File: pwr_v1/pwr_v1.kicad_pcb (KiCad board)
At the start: 4 copper layers, 166 x 166 mm, 118 parts, among them CN11 Conn_02x36_Odd_Even, CN12 Conn_02x36_Odd_Even, M1 Conn_01x08_Socket, M2 Conn_01x08_Socket, M3 Conn_01x08_Socket, M4 Conn_01x08_Socket, M5 Conn_01x08_Socket, U1 LM2576S-5, U2 LM2576S-12, U4 LSM6DSLTR

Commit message: Schematic and layout updated; Layout placement and routing completed
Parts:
- removed the REF** at (118.0, 65.1)
- added 0R1: 0, Resistor_SMD:R_0603_1608Metric, F.Cu at (187.4, 125.0)
- added 0R10: 0, Resistor_SMD:R_0603_1608Metric, F.Cu at (126.8, 104.0)
- added 0R11: 0, Resistor_SMD:R_0603_1608Metric, F.Cu at (187.6, 119.4)
- added 0R12: 0, Resistor_SMD:R_0603_1608Metric, F.Cu at (173.2, 119.2)
- added 0R13: 0, Resistor_SMD:R_0603_1608Metric, F.Cu at (171.8, 128.6)
- added 0R14: 0, Resistor_SMD:R_0603_1608Metric, F.Cu at (127.2, 98.1)
- added 0R15: 0, Resistor_SMD:R_0603_1608Metric, F.Cu at (171.8, 131.1)
- added 0R16: 0, Resistor_SMD:R_0603_1608Metric, F.Cu at (126.2, 120.1)
- added 0R17: 0, Resistor_SMD:R_0603_1608Metric, F.Cu at (127.1, 125.9)
- added 0R18: 0, Resistor_SMD:R_0603_1608Metric, F.Cu at (111.4, 85.4)
- added 0R19: 0, Resistor_SMD:R_0603_1608Metric, F.Cu at (127.0, 123.5)
- added 0R2: 0, Resistor_SMD:R_0603_1608Metric, F.Cu at (127.0, 67.7)
- added 0R20: 0, Resistor_SMD:R_0603_1608Metric, F.Cu at (127.2, 141.3)
- added 0R21: 0, Resistor_SMD:R_0603_1608Metric, F.Cu at (173.2, 81.2)
- added 0R22: 0, Resistor_SMD:R_0603_1608Metric, F.Cu at (172.4, 77.8)
- added 0R23: 0, Resistor_SMD:R_0603_1608Metric, F.Cu at (171.8, 100.6)
- added 0R24: 0, Resistor_SMD:R_0603_1608Metric, F.Cu at (187.4, 94.6)
- added 0R25: 0, Resistor_SMD:R_0603_1608Metric, F.Cu at (187.6, 68.4)
- added 0R26: 0, Resistor_SMD:R_0603_1608Metric, F.Cu at (172.6, 67.6)
- added 0R27: 0, Resistor_SMD:R_0603_1608Metric, F.Cu at (188.0, 80.4)
- added 0R28: 0, Resistor_SMD:R_0603_1608Metric, F.Cu at (188.4, 77.8)
- added 0R29: 0, Resistor_SMD:R_0603_1608Metric, F.Cu at (127.2, 100.7)
- added 0R3: 0, Resistor_SMD:R_0603_1608Metric, F.Cu at (173.0, 86.4)
- added 0R30: 0, Resistor_SMD:R_0603_1608Metric, F.Cu at (172.2, 111.0)
- added 0R31: 0, Resistor_SMD:R_0603_1608Metric, F.Cu at (172.2, 108.4)
- added 0R32: 0, Resistor_SMD:R_0603_1608Metric, F.Cu at (187.4, 101.4)
- added 0R33: 0, Resistor_SMD:R_0603_1608Metric, F.Cu at (188.2, 85.4)
- added 0R34: 0, Resistor_SMD:R_0603_1608Metric, F.Cu at (172.2, 95.6)
- added 0R35: 0, Resistor_SMD:R_0603_1608Metric, F.Cu at (188.2, 83.0)
- added 0R36: 0, Resistor_SMD:R_0603_1608Metric, F.Cu at (171.8, 126.0)
- added 0R4: 0, Resistor_SMD:R_0603_1608Metric, F.Cu at (187.4, 90.6)
- added 0R5: 0, Resistor_SMD:R_0603_1608Metric, F.Cu at (187.4, 132.8)
- added 0R6: 0, Resistor_SMD:R_0603_1608Metric, F.Cu at (187.8, 143.0)
- added 0R7: 0, Resistor_SMD:R_0603_1608Metric, F.Cu at (187.2, 112.4)
- added 0R8: 0, Resistor_SMD:R_0603_1608Metric, F.Cu at (172.2, 116.0)
- added 0R9: 0, Resistor_SMD:R_0603_1608Metric, F.Cu at (171.8, 133.8)
- added ?: , , B.Cu at (215.0, 136.2)
- added ?: , , B.Cu at (180.2, 37.8)
- added ?: , , B.Cu at (83.0, 84.0)
- added ?: , , B.Cu at (134.8, 164.4)
- added Bat2: Conn_01x07, B7B_XH_A:JST_B7B-XH-A, F.Cu at (151.6, 153.6)
- added C5: 100uF, Capacitor_SMD:CP_Elec_8x10, B.Cu at (140.1, 128.6)
- added C6: 1000uF, Capacitor_SMD:CP_Elec_10x10.5, B.Cu at (160.4, 118.1)
- added D3: 1N5821, Diode_THT:D_DO-201AD_P15.24mm_Horizontal, B.Cu at (148.4, 119.3)
- added J1: Conn_01x12_Pin, 12pConn:CON12_1X12_UR_DF13, B.Cu at (222.1, 127.8)
- added L4: 100uH, Inductor_SMD:L_Sunlord_MWSA1206S-101, B.Cu at (147.4, 107.5)
- added Q1: BSS84, Package_TO_SOT_SMD:SOT-23, B.Cu at (215.0, 126.5)
- added R15: 1M, Resistor_SMD:R_0603_1608Metric, F.Cu at (171.0, 146.4)
- added R16: 100k, Resistor_SMD:R_0603_1608Metric, F.Cu at (171.0, 148.0)
- added REF**: TerminalBlock_MetzConnect_360271_1x01_Horizontal_ScrewM3.0_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, TerminalBlock_MetzConnect:TerminalBlock_MetzConnect_360271_1x01_Horizontal_ScrewM3.0_Boxed, F.Cu at (120.0, 36.0)
- added REF**: Fiducial_1mm_Mask2mm, Fiducial:Fiducial_1mm_Mask2mm, F.Cu at (83.0, 84.0)
- added REF**: Fiducial_1mm_Mask2mm, Fiducial:Fiducial_1mm_Mask2mm, F.Cu at (180.2, 37.8)
- added REF**: Fiducial_1mm_Mask2mm, Fiducial:Fiducial_1mm_Mask2mm, F.Cu at (215.0, 136.2)
- added REF**: TerminalBlock_MetzConnect_360271_1x01_Horizontal_ScrewM3.0_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, TerminalBlock_MetzConnect:TerminalBlock_MetzConnect_360271_1x01_Horizontal_ScrewM3.0_Boxed, F.Cu at (180.4, 164.0)
- added REF**: TerminalBlock_MetzConnect_360271_1x01_Horizontal_ScrewM3.0_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, TerminalBlock_MetzConnect:TerminalBlock_MetzConnect_360271_1x01_Horizontal_ScrewM3.0_Boxed, F.Cu at (119.4, 163.8)
- added REF**: TerminalBlock_MetzConnect_360271_1x01_Horizontal_ScrewM3.0_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, TerminalBlock_MetzConnect:TerminalBlock_MetzConnect_360271_1x01_Horizontal_ScrewM3.0_Boxed, F.Cu at (188.4, 36.0)
- added REF**: Fiducial_1mm_Mask2mm, Fiducial:Fiducial_1mm_Mask2mm, F.Cu at (134.8, 164.4)
- added RK1: 100, Resistor_SMD:R_0402_1005Metric, B.Cu at (219.7, 127.8)
- added RK10: 10k, Resistor_SMD:R_0402_1005Metric, B.Cu at (216.5, 120.2)
- added RK2: 100, Resistor_SMD:R_0402_1005Metric, B.Cu at (219.6, 126.5)
- added RK3: 100, Resistor_SMD:R_0402_1005Metric, B.Cu at (219.6, 125.3)
- added RK4: 100, Resistor_SMD:R_0402_1005Metric, B.Cu at (219.7, 124.1)
- added RK5: 100, Resistor_SMD:R_0402_1005Metric, B.Cu at (219.6, 122.7)
- added RK6: 100, Resistor_SMD:R_0402_1005Metric, B.Cu at (219.8, 121.5)
- added RK7: 100, Resistor_SMD:R_0402_1005Metric, B.Cu at (219.8, 120.3)
- added RK8: 100, Resistor_SMD:R_0402_1005Metric, B.Cu at (219.8, 118.9)
- added RK9: 10k, Resistor_SMD:R_0402_1005Metric, B.Cu at (216.5, 121.5)
- added U3: LM2576S-3.3, Package_TO_SOT_SMD:TO-263-5_TabPin3, B.Cu at (152.0, 133.3)
- J_IR1: footprint Connector_PinHeader_2.54mm:PinHeader_1x05_P2.54mm_Vertical -> Connector_PinHeader_2.54mm:PinHeader_1x05_P2.54mm_Vertical_SMD_Pin1Left; moved to B.Cu
- J_RF1: footprint Connector_PinHeader_2.54mm:PinHeader_2x04_P2.54mm_Vertical -> Connector_PinSocket_2.54mm:PinSocket_2x04_P2.54mm_Vertical
- M1, M2, M3, M4, M5: footprint Connector_Molex:Molex_KK-254_AE-6410-08A_1x08_P2.54mm_Vertical -> Connector_PinHeader_2.54mm:PinHeader_1x08_P2.54mm_Vertical; moved to B.Cu
- moved C1 139.7 mm to (217.5, 87.9), turned to 0 degrees
- moved U1 138.9 mm to (76.5, 98.0), turned to 180 degrees
- moved U2 132.6 mm to (222.3, 99.9), turned to 0 degrees
- moved C3 130.8 mm to (93.6, 90.0), turned to 90 degrees
- moved R14 127.9 mm to (156.6, 148.0), turned to 90 degrees
- moved R13 127.4 mm to (156.7, 144.8), turned to -90 degrees
- moved R12 127.2 mm to (154.1, 148.0), turned to 90 degrees
- moved R10 126.8 mm to (151.6, 147.9), turned to 90 degrees
- moved R4 126.8 mm to (144.1, 147.9), turned to 90 degrees
- moved R11 126.7 mm to (154.2, 144.8), turned to -90 degrees
- moved R8 126.7 mm to (149.2, 148.0), turned to 90 degrees
- moved R6 126.5 mm to (146.6, 148.0), turned to 90 degrees
- moved R9 126.2 mm to (151.6, 144.8), turned to -90 degrees
- moved R7 125.9 mm to (149.2, 144.8), turned to -90 degrees
- moved R1 125.9 mm to (144.1, 144.8), turned to -90 degrees
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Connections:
- C12 pad 1: /3V3 -> 3V3
- C13 pad 1: /3V3 -> 3V3
- CN11 pad 11: unconnected-(CN11-Pin_11-Pad11) -> /Battery Supervisor/O1
- CN11 pad 17: unconnected-(CN11-Pin_17-Pad17) -> /STM32/MOTOR5_ENCODER
- CN11 pad 19: unconnected-(CN11-Pin_19-Pad19) -> GND
- CN11 pad 22: unconnected-(CN11-Pin_22-Pad22) -> GND
- CN11 pad 23: /STM32/BTN_USER -> unconnected-(CN11-Pin_23-Pad23)
- CN11 pad 28: unconnected-(CN11-Pin_28-Pad28) -> /STM32/MOTOR4_ENCODER
- CN11 pad 30: unconnected-(CN11-Pin_30-Pad30) -> /STM32/IR_CS
- CN11 pad 32: unconnected-(CN11-Pin_32-Pad32) -> /STM32/MOTOR3_ENCODER
- CN11 pad 34: /STM32/LED_GREEN -> unconnected-(CN11-Pin_34-Pad34)
- CN11 pad 38: unconnected-(CN11-Pin_38-Pad38) -> /Battery Supervisor/O6
- CN11 pad 4: unconnected-(CN11-Pin_4-Pad4) -> /STM32/MOTOR1_ENCODER
- CN11 pad 46: /MotorDriver4/BRAKE -> /STM32/MOTOR4_BREAK
- CN11 pad 48: unconnected-(CN11-Pin_48-Pad48) -> /STM32/MOTOR5_REVERSE
- CN11 pad 49: unconnected-(CN11-Pin_49-Pad49) -> GND
- CN11 pad 50: unconnected-(CN11-Pin_50-Pad50) -> /STM32/MOTOR5_PWM
- CN11 pad 54: unconnected-(CN11-Pin_54-Pad54) -> /Battery Supervisor/O3
- CN11 pad 56: unconnected-(CN11-Pin_56-Pad56) -> /Battery Supervisor/O2
- CN11 pad 60: unconnected-(CN11-Pin_60-Pad60) -> GND
- CN11 pad 61: /STM32/LED_YELLOW -> unconnected-(CN11-Pin_61-Pad61)
- CN11 pad 62: unconnected-(CN11-Pin_62-Pad62) -> /STM32/MOTOR5_BREAK
- CN11 pad 8: unconnected-(CN11-Pin_8-Pad8) -> GND
- CN11 pad 9: /MotorDriver1/FGOUT -> /Battery Supervisor/O4
- CN12 pad 11: /SCK -> /STM32/SCK
- CN12 pad 12: unconnected-(CN12-Pin_12-Pad12) -> /STM32/IR_IN
- CN12 pad 13: /MISO -> /STM32/MISO
- CN12 pad 14: unconnected-(CN12-Pin_14-Pad14) -> /STM32/IR_OUT
- CN12 pad 15: /MOSI -> unconnected-(CN12-Pin_15-Pad15)
- CN12 pad 16: unconnected-(CN12-Pin_16-Pad16) -> /STM32/KICKER_DISCHARGE2
- CN12 pad 17: /MotorDriver1/DIR -> /STM32/MOTOR1_REVERSE
- CN12 pad 18: unconnected-(CN12-Pin_18-Pad18) -> /STM32/KICKER_CHARGE
- CN12 pad 20: unconnected-(CN12-Pin_20-Pad20) -> GND
- CN12 pad 22: /MotorDriver1/BRAKE -> /STM32/MOTOR1_BREAK
- CN12 pad 23: /MotorDriver1/PWM -> unconnected-(CN12-Pin_23-Pad23)
- CN12 pad 25: /STM32/KICKER_DISCHARGE -> /STM32/KICKER_DISCHARGE1
- CN12 pad 26: /RF/IRQ -> /STM32/NRF_IRQ
- CN12 pad 28: /STM32/LED_RED -> unconnected-(CN12-Pin_28-Pad28)
- CN12 pad 29: unconnected-(CN12-Pin_29-Pad29) -> /STM32/MOSI
- CN12 pad 3: /RF/CSN -> /STM32/CS_NRF
- CN12 pad 30: /MotorDriver2/DIR -> /STM32/KICKER_ERR
- CN12 pad 35: /MotorDriver3/FGOUT -> /STM32/IR_INT1
- CN12 pad 37: unconnected-(CN12-Pin_37-Pad37) -> /STM32/IR_INT2
- CN12 pad 39: unconnected-(CN12-Pin_39-Pad39) -> GND
- CN12 pad 4: /RF/CE -> /STM32/CE_NRF
- CN12 pad 40: unconnected-(CN12-Pin_40-Pad40) -> /STM32/MOTOR2_REVERSE
- CN12 pad 41: /MotorDriver2/BRAKE -> /STM32/MOTOR2_BREAK
- CN12 pad 42: /MotorDriver2/FGOUT -> /Battery Supervisor/O5
- CN12 pad 43: /MotorDriver3/BRAKE -> /STM32/MOTOR3_BREAK
- CN12 pad 44: /MotorDriver3/DIR -> /STM32/MOTOR3_REVERSE
- CN12 pad 47: /MotorDriver4/DIR -> unconnected-(CN12-Pin_47-Pad47)
- CN12 pad 49: unconnected-(CN12-Pin_49-Pad49) -> /STM32/KICKER_CS
- CN12 pad 51: /MotorDriver3/PWM -> /STM32/MOTOR4_PWM
- CN12 pad 52: unconnected-(CN12-Pin_52-Pad52) -> /STM32/MOTOR1_PWM
- CN12 pad 53: unconnected-(CN12-Pin_53-Pad53) -> /STM32/MOTOR4_REVERSE
- CN12 pad 54: unconnected-(CN12-Pin_54-Pad54) -> GND
- CN12 pad 55: /MotorDriver4/PWM -> /STM32/MOTOR3_PWM
- CN12 pad 56: /MotorDriver2/PWM -> /STM32/MOTOR2_PWM
- CN12 pad 63: unconnected-(CN12-Pin_63-Pad63) -> GND
- CN12 pad 64: unconnected-(CN12-Pin_64-Pad64) -> /STM32/MOTOR2_ENCODER
- CN12 pad 65: unconnected-(CN12-Pin_65-Pad65) -> /Battery Supervisor/M
- CN12 pad 70: /MotorDriver4/FGOUT -> unconnected-(CN12-Pin_70-Pad70)
- CN12 pad 9: unconnected-(CN12-Pin_9-Pad9) -> GND
- J_IR1 pad 1: /3V3 -> /IR/IR_IN
- J_IR1 pad 2: /3V3 -> GND
- J_IR1 pad 3: GND -> 3V3
- J_RF1 pad 8: /3V3 -> 3V3
- R1 pad 1: /Battery Supervisor/B1 -> /Battery Supervisor/P
- R10 pad 1: /Battery Supervisor/G -> /Battery Supervisor/B4
- R11 pad 1: /Battery Supervisor/B5 -> /Battery Supervisor/P
- R12 pad 1: /Battery Supervisor/G -> /Battery Supervisor/B5
- R13 pad 1: /Battery Supervisor/B6 -> /Battery Supervisor/P
- R14 pad 1: /Battery Supervisor/G -> /Battery Supervisor/B6
- R2 pad 1: /3V3 -> 3V3
- R2 pad 2: /IMU/SCL -> /SCK
- R3 pad 1: /3V3 -> 3V3
- R3 pad 2: /IMU/SDA -> /MOSI
- R4 pad 1: /Battery Supervisor/G -> /Battery Supervisor/B1
- R5 pad 1: /Battery Supervisor/B2 -> /Battery Supervisor/P
- R6 pad 1: /Battery Supervisor/G -> /Battery Supervisor/B2
- R7 pad 1: /Battery Supervisor/B3 -> /Battery Supervisor/P
- R8 pad 1: /Battery Supervisor/G -> /Battery Supervisor/B3
- R9 pad 1: /Battery Supervisor/B4 -> /Battery Supervisor/P
- U4 pad 1: /IMU/SDO/SA0 -> /MISO
- U4 pad 13: /IMU/SCL -> /SCK
- U4 pad 14: /IMU/SDA -> /MOSI
- U4 pad 5: /3V3 -> 3V3
- U4 pad 8: /3V3 -> 3V3
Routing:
- net 5V: track 16.7 -> 373.7 mm, vias 10 -> 29
- net /SCK: track 0.00 -> 207.6 mm, vias 0 -> 5
- net /MISO: track 0.00 -> 192.8 mm, vias 0 -> 2
- net /MOSI: track 0.00 -> 188.3 mm, vias 0 -> 5
- net /MotorDriver2/FGOUT: track 5.73 -> 155.6 mm, vias 0 -> 1
- net /MotorDriver2/PWM: track 2.60 -> 148.6 mm
- net /MotorDriver4/BRAKE: track 4.11 -> 144.3 mm, vias 1 -> 3
- net 3V3: track 0.00 -> 132.1 mm, vias 0 -> 24
- net /MotorDriver2/DIR: track 2.03 -> 133.0 mm
- net /RF/IRQ: track 0.00 -> 122.3 mm, vias 0 -> 1
- net /MotorDriver3/DIR: track 2.04 -> 117.6 mm
- net /MotorDriver5/BRAKE: track 4.11 -> 116.9 mm
- net /MotorDriver2/BRAKE: track 4.11 -> 115.9 mm
- net /Battery Supervisor/O4: track 2.08 -> 109.2 mm, vias 1 -> 2
- net /MotorDriver5/DIR: track 2.04 -> 104.8 mm
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- added copper zone on In2.Cu, net 3V3
- added copper zone on In2.Cu, net 5V
- added copper zone on In1.Cu, net GND
- added copper zone on In2.Cu, net VBAT
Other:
- board text added: "XT60"

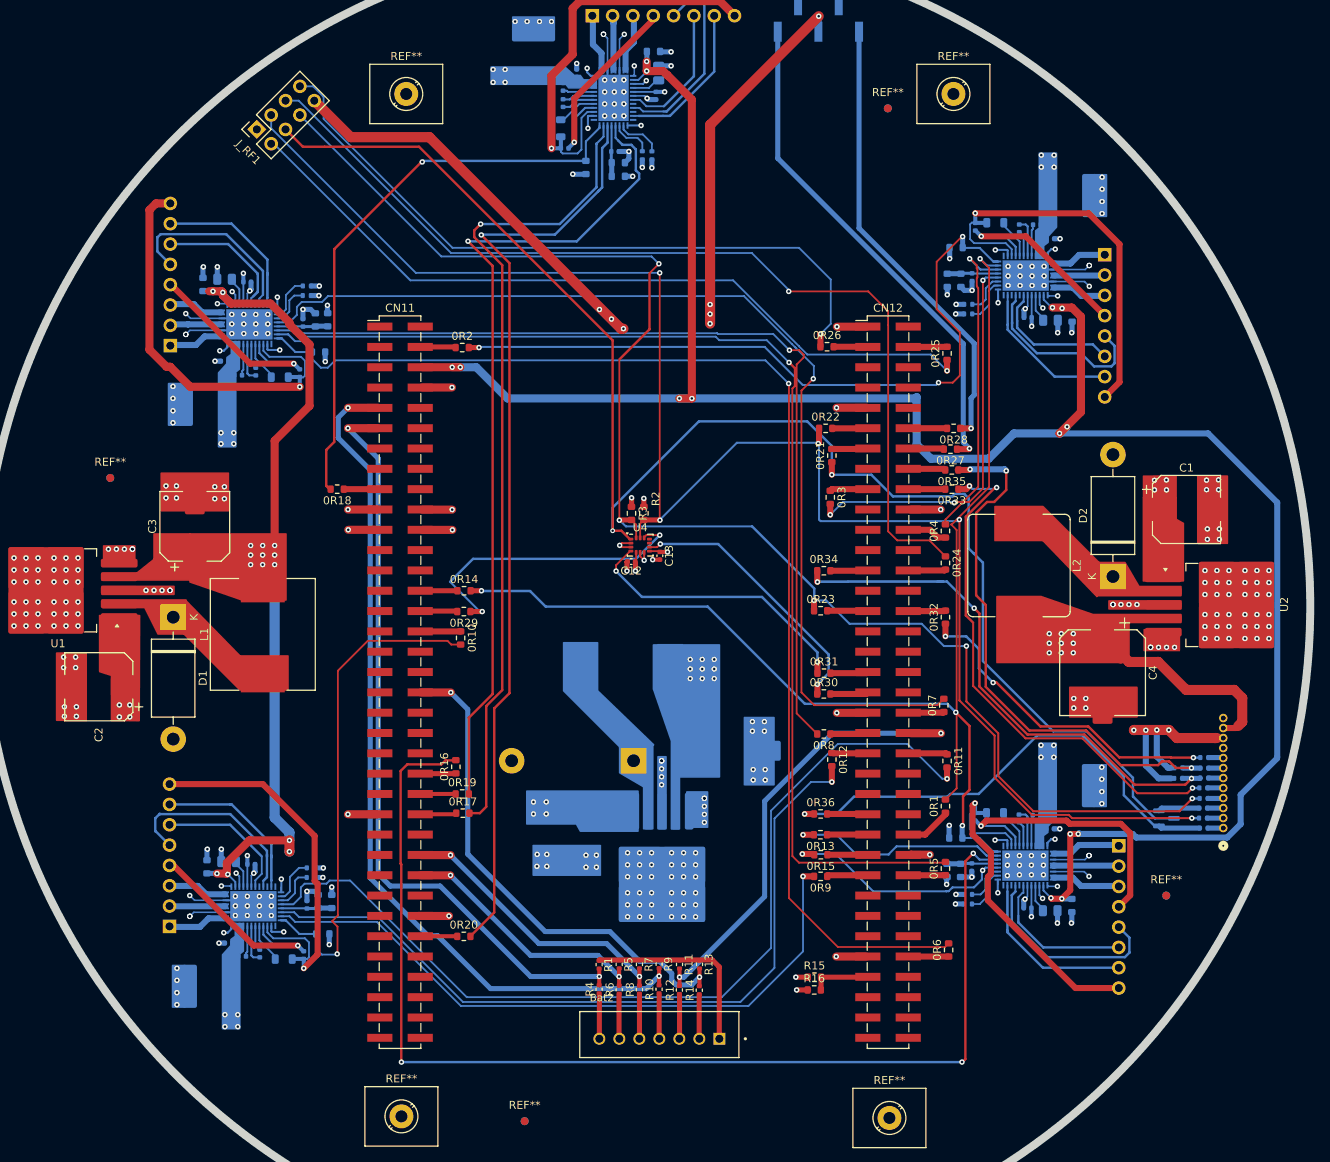
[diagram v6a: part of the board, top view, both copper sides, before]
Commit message: Sch: Mechanical comp added; Lay: SIlkscreen aligned, trace widths updated to atleast 12 mils.
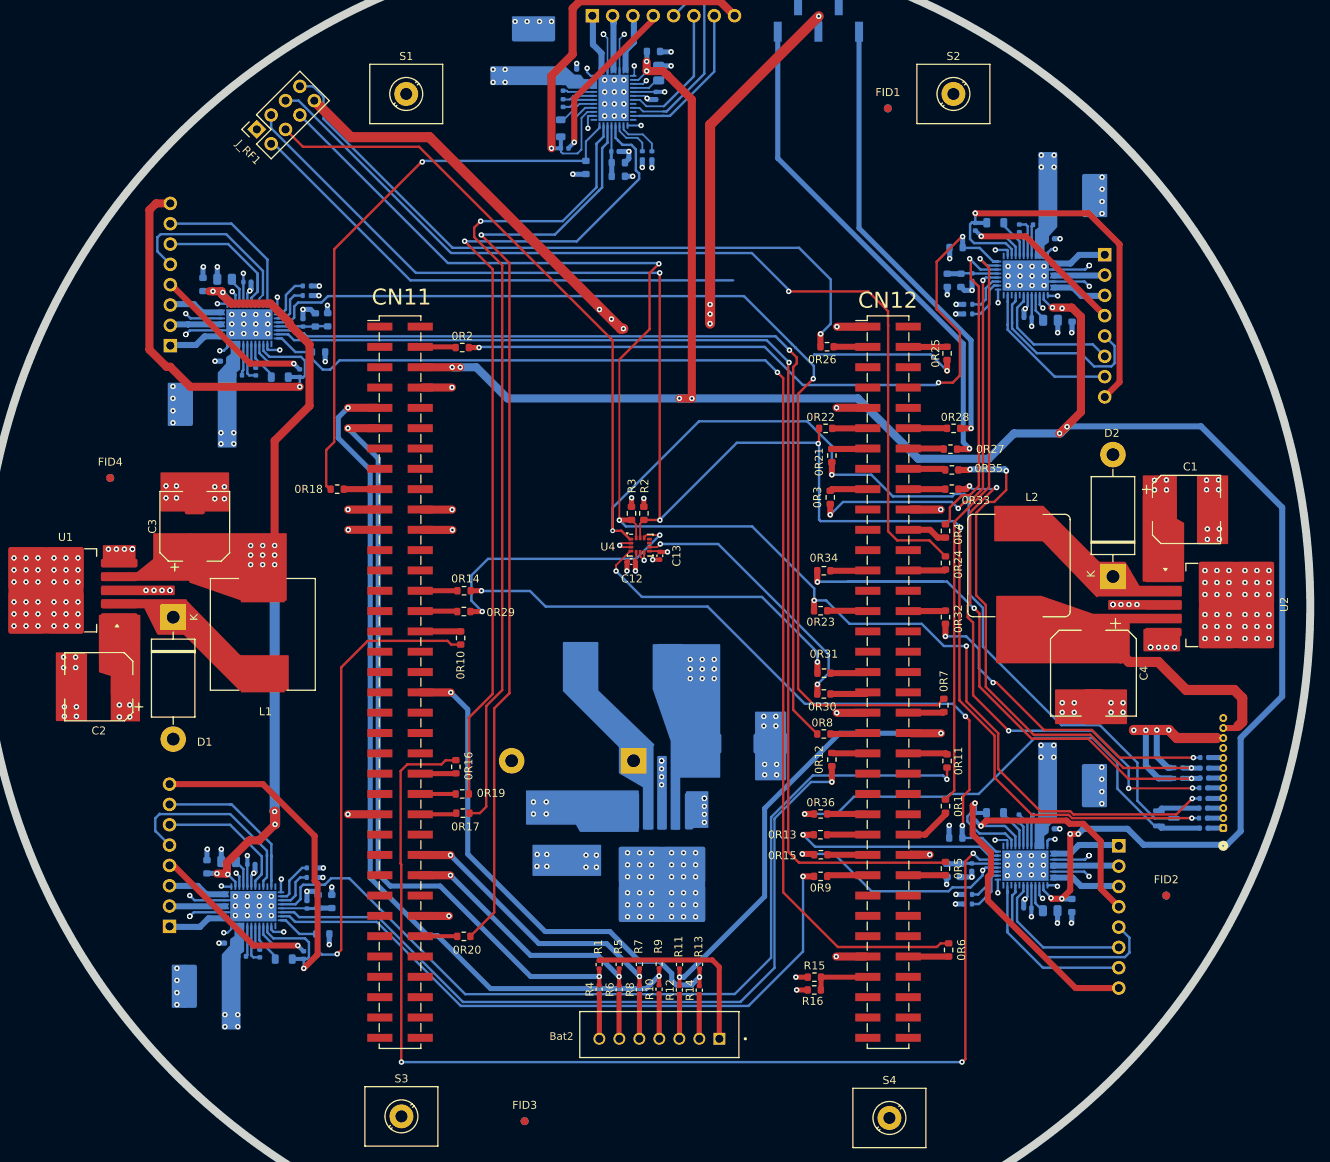
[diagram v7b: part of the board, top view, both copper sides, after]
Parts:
- FID1, FID2, FID3, FID4: renamed from REF**; value Fiducial_1mm_Mask2mm -> Fiducial
- S1, S2, S3, S4: renamed from REF**; value TerminalBlock_MetzConnect_360271_1x01_Horizontal_ScrewM3.0_Boxed -> Screw_Terminal_01x01
- moved C6 1.33 mm to (161.4, 117.2)
- moved C4 1.14 mm to (205.9, 108.4)
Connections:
- S1 pad 1: (no net) -> GND
- S2 pad 1: (no net) -> GND
- S3 pad 1: (no net) -> GND
- S4 pad 1: (no net) -> GND
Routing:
- net /RF/CE: track 97.6 -> 83.7 mm
- net 5V: track 373.7 -> 369.3 mm
- net /MotorDriver4/GND_BK: track 36.3 -> 32.5 mm
- net GND: track 190.5 -> 186.8 mm, vias 325 -> 329
- net /IMU/CS: track 37.8 -> 34.3 mm
- net /MotorDriver1/H2: track 26.6 -> 23.4 mm
- net /MotorDriver4/H3: track 24.6 -> 21.5 mm
- net /MotorDriver2/H3: track 22.7 -> 19.6 mm
- net /MotorDriver3/DIR: track 117.6 -> 114.8 mm
- net /MotorDriver4/H2: track 27.8 -> 25.6 mm
- net /MotorDriver4/DIR: track 29.6 -> 31.4 mm
- net /MotorDriver1/AVDD: track 16.4 -> 14.6 mm
- net /MotorDriver2/PWM: track 148.6 -> 146.9 mm
- net /KB/CHG: track 66.2 -> 67.8 mm, vias 3 -> 5
- net /MotorDriver2/BRAKE: track 115.9 -> 114.9 mm
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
